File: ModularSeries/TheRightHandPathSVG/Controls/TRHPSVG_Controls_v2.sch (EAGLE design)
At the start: 56 parts, among them IC2 LM358

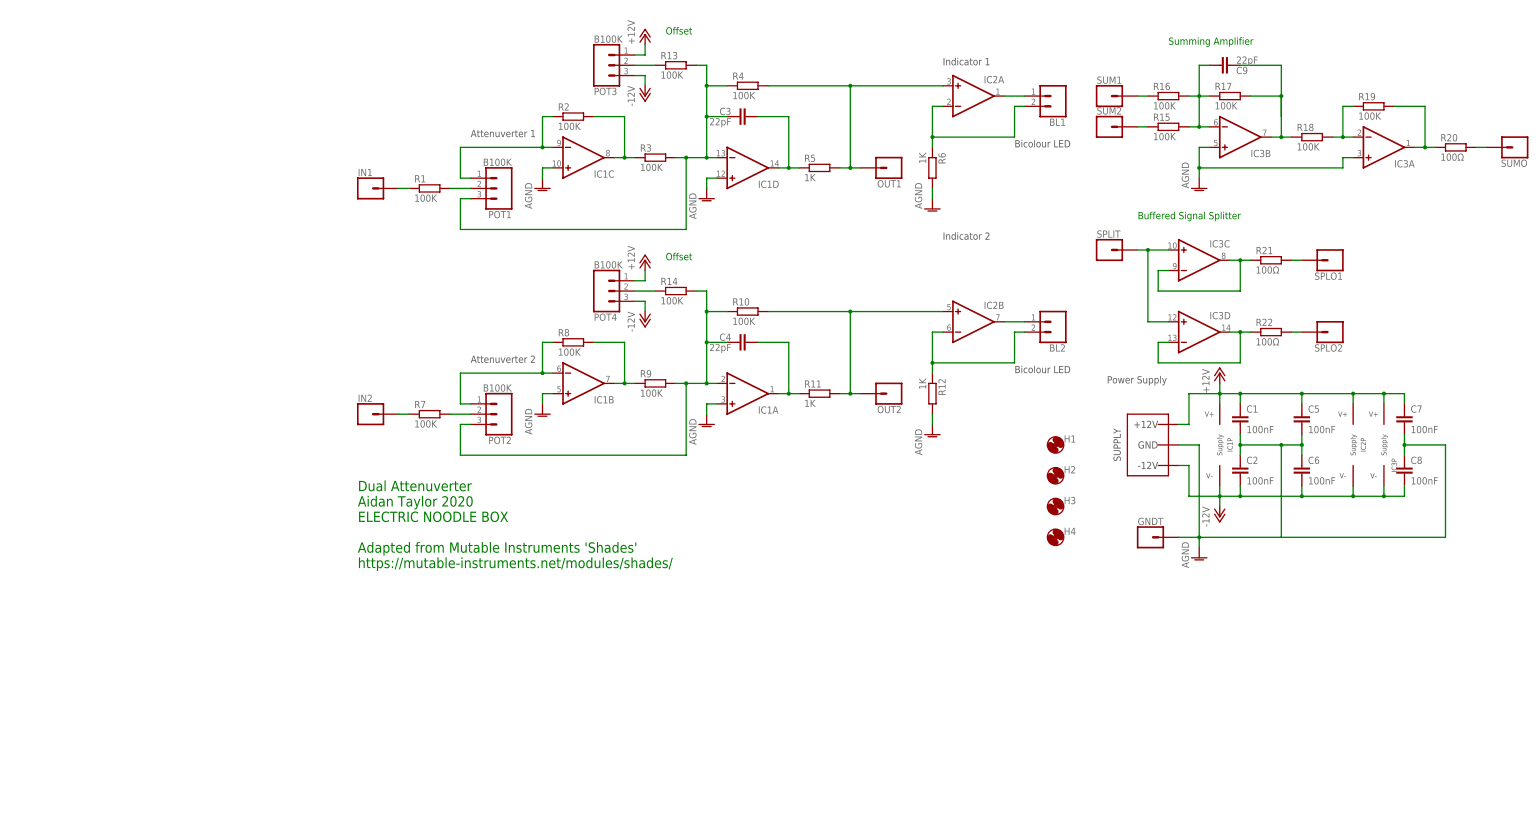
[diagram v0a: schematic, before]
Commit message: TRHP-SVG version 2, Endings added and Mirrors updated
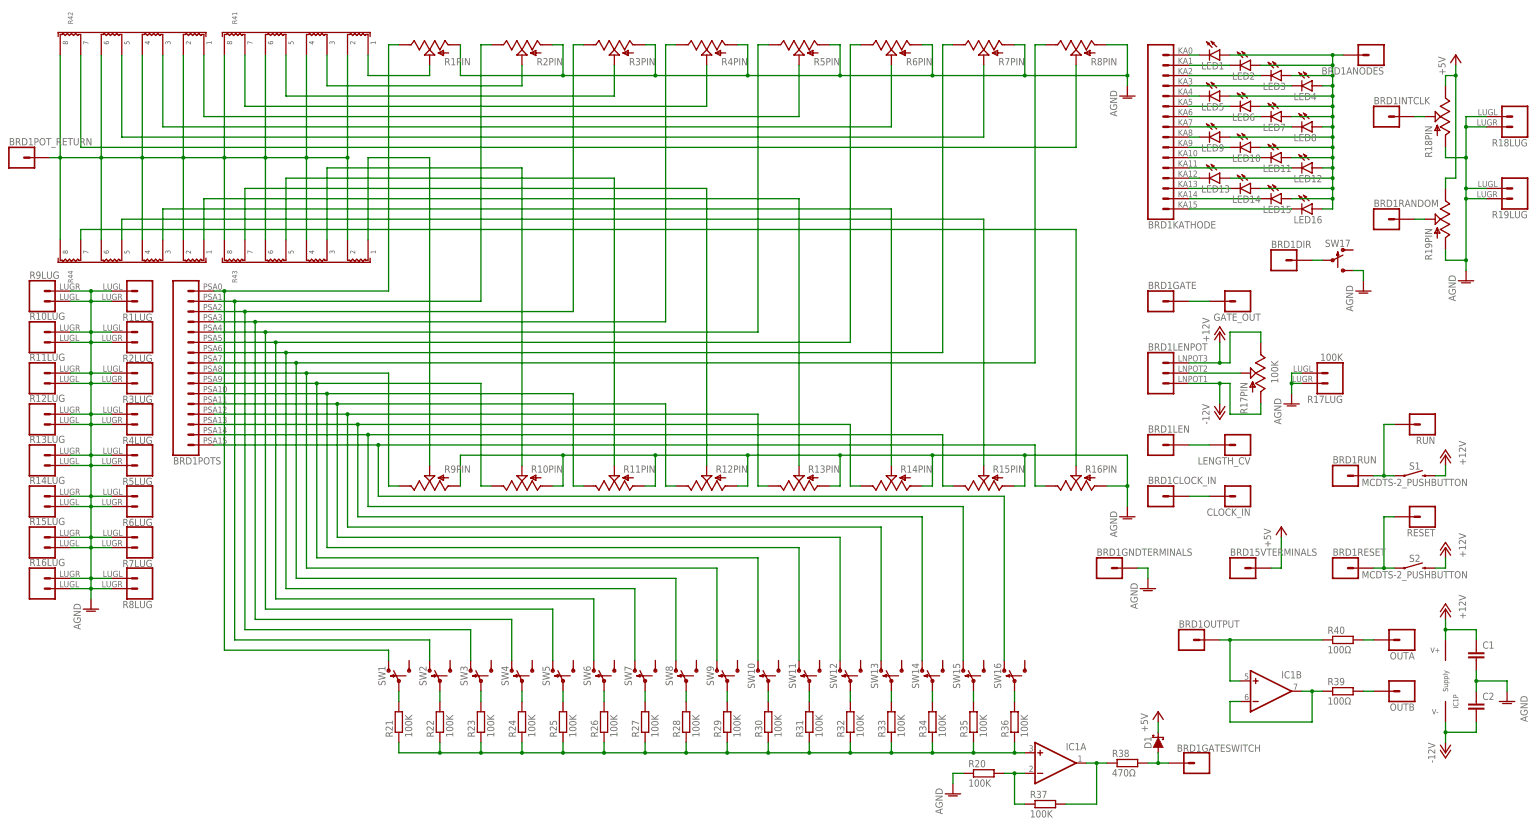
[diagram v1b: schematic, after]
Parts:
- removed BL1, BL2: 2XWIREPAD, ElectricNoodleBox:2XWIREPAD
- removed C3, C4, C9: 22pF, rcl:C-EU050-025X075
- removed C5, C6, C7, C8: 100nF, rcl:C-EU050-025X075
- removed GNDT, IN1, IN2, OUT1, OUT2, SPLIT, SPLO1, SPLO2, SUM1, SUM2, SUMO: 1XWIREPAD, ElectricNoodleBox:1XWIREPAD
- removed H1, H2, H3, H4: MOUNT-HOLE3.2, holes:MOUNT-HOLE3.2
- removed IC2: LM358, ElectricNoodleBox:LM358
- removed IC3: (no value), ElectricNoodleBox:TL0X4DIL
- removed POT1, POT2, POT3, POT4: B100K, ElectricNoodleBox:3XWIREPAD
- removed WP1: COMBO_SUPPLY_HEADER, ElectricNoodleBox:COMBO_SUPPLY_HEADER
- added BRD1: TRHPSVG_LINK, ElectricNoodleBox:TRHPSVG_LINK
- added CLOCK_IN, GATE_OUT, LENGTH_CV, OUTA, OUTB, RESET, RUN: BANANA_PANEL, ElectricNoodleBox:BANANA_PANEL
- added D1: (no value), ElectricNoodleBox:SCHOTTKY_DO35
- added LED1, LED10, LED11, LED12, LED13, LED14, LED15, LED16, LED2, LED3, LED4, LED5, LED6, LED7, LED8, LED9: (no value), led:LED3MM
- added R23, R24, R25, R26, R27, R28, R29, R30, R31, R32, R33, R34, R35, R36, R37: 100K, rcl:R-EU_0207/10
- added R38: 470Ω, rcl:R-EU_0207/10
- added R39, R40: 100Ω, rcl:R-EU_0207/10
- added R41, R42, R43, R44: (no value), ElectricNoodleBox:4XISO_RESISTOR_NETWORK_2.54
- added S1, S2: MCDTS-2_PUSHBUTTON, ElectricNoodleBox:MCDTS-2_PUSHBUTTON
- added SW1, SW10, SW11, SW12, SW13, SW14, SW15, SW16, SW17, SW2, SW3, SW4, SW5, SW6, SW7, SW8, SW9: SPDT_SWITCHDW1, ElectricNoodleBox:SPDT_SWITCHDW1
- C1, C2: value 100nF -> (none)
- IC1: device ElectricNoodleBox:TL0X4DIL -> ElectricNoodleBox:TL0X2DIL
- R1, R10, R13, R14, R15, R16, R18, R19, R2, R3, R4, R7, R8, R9: value 100K -> (none); device rcl:R-EU_0207/10 -> ElectricNoodleBox:POTENTIOMETER
- R11, R12, R5, R6: value 1K -> (none); device rcl:R-EU_0207/10 -> ElectricNoodleBox:POTENTIOMETER
- R17: device rcl:R-EU_0207/10 -> ElectricNoodleBox:POTENTIOMETER
- R20, R21, R22: value 100Ω -> 100K
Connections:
- new net +5V: BRD15VTERMINALS.1, D1.C, R18PIN.B, R19PIN.B
- new net N$33: BRD1KATHODE.1, LED1.C
- new net N$34: BRD1ANODES.1, LED1.A, LED10.A, LED11.A, LED12.A, LED13.A, LED14.A, LED15.A, LED16.A, LED2.A, LED3.A, LED4.A, LED5.A, LED6.A, LED7.A, LED8.A, LED9.A
- new net N$35: BRD1KATHODE.2, LED2.C
- new net N$36: BRD1KATHODE.3, LED3.C
- new net N$37: BRD1KATHODE.4, LED4.C
- new net N$38: BRD1KATHODE.5, LED5.C
- new net N$39: BRD1KATHODE.6, LED6.C
- new net N$40: BRD1KATHODE.7, LED7.C
- new net N$41: BRD1KATHODE.8, LED8.C
- new net N$42: BRD1KATHODE.9, LED9.C
- new net N$43: BRD1KATHODE.10, LED10.C
- new net N$44: BRD1KATHODE.11, LED11.C
- new net N$45: BRD1KATHODE.12, LED12.C
- new net N$46: BRD1KATHODE.13, LED13.C
- new net N$47: BRD1KATHODE.14, LED14.C
- new net N$48: BRD1KATHODE.15, LED15.C
- new net N$49: BRD1KATHODE.16, LED16.C
- new net N$50: BRD1LEN.1, LENGTH_CV.1
- new net N$51: BRD1CLOCK_IN.1, CLOCK_IN.1
- new net N$52: BRD1OUTPUT.1, IC1B.+IN, R40.1
- new net N$53: BRD1GATE.1, GATE_OUT.1
- new net N$54: BRD1DIR.1, SW17.P
- new net N$55: BRD1LENPOT.2, R17PIN.W
- new net N$56: BRD1POTS.6, R6PIN.B, SW6.O
- new net N$57: BRD1INTCLK.1, R18PIN.W
- new net N$58: BRD1RANDOM.1, R19PIN.W
- new net N$59: BRD1RUN.1, RUN.1, S1.1
- new net N$60: BRD1RESET.1, RESET.1, S2.1
- new net N$61: R26.2, SW6.P
- new net N$62: R27.2, SW7.P
- new net N$63: R28.2, SW8.P
- new net N$64: R29.2, SW9.P
- new net N$65: R30.2, SW10.P
- new net N$66: R31.2, SW11.P
- new net N$67: R32.2, SW12.P
- new net N$68: R33.2, SW13.P
- new net N$69: BRD1POTS.9, R9PIN.B, SW9.O
- new net N$70: BRD1POTS.11, R11PIN.B, SW11.O
- new net N$71: BRD1POTS.10, R10PIN.B, SW10.O
- new net N$72: BRD1POTS.13, R13PIN.B, SW13.O
- new net N$73: BRD1POTS.12, R12PIN.B, SW12.O
- new net N$74: R34.2, SW14.P
- new net N$75: R35.2, SW15.P
- new net N$76: IC1A.+IN, R21.1, R22.1, R23.1, R24.1, R25.1, R26.1, R27.1, R28.1, R29.1, R30.1, R31.1, R32.1, R33.1, R34.1, R35.1, R36.1
- new net N$77: IC1A.-IN, R20.2, R37.1
- new net N$78: IC1A.OUT, R37.2, R38.1
- new net N$79: BRD1GATESWITCH.1, D1.A, R38.2
- new net N$80: IC1B.-IN, IC1B.OUT, R39.1
- new net N$81: OUTB.1, R39.2
- new net N$82: OUTA.1, R40.2
- new net N$83: BRD1POT_RETURN.1, R41.P$2, R41.P$4, R41.P$6, R41.P$8, R42.P$2, R42.P$4, R42.P$6, R42.P$8, R43.P$2, R43.P$4, R43.P$6, R43.P$8, R44.P$2, R44.P$4, R44.P$6, R44.P$8
- net +12V: now also BRD1LENPOT.3, R17PIN.B, S1.2, S2.2; no longer C5.1, C7.1, IC2P.V+, IC3P.V+, POT3.1, POT4.1, WP1.V++
- net -12V: now also BRD1LENPOT.1, R17PIN.A; no longer C6.2, C8.2, IC2P.V-, IC3P.V-, POT3.3, POT4.3, WP1.V--
- net AGND: now also BRD1GNDTERMINALS.1, R10LUG.1, R10LUG.2, R10PIN.A, R11LUG.1, R11LUG.2, R11PIN.A, R12LUG.1, R12LUG.2, R12PIN.A, R13LUG.1, R13LUG.2, R13PIN.A, R14LUG.1, R14LUG.2, R14PIN.A, R15LUG.1, R15LUG.2, R15PIN.A, R16LUG.1, R16LUG.2, R16PIN.A, R17LUG.1, R17LUG.2, R18LUG.1, R18LUG.2, R18PIN.A, R19LUG.1, R19LUG.2, R19PIN.A, R1LUG.1, R1LUG.2, R1PIN.A, R20.1, R2LUG.1, R2LUG.2, R2PIN.A, R3LUG.1, R3LUG.2, R3PIN.A, R4LUG.1, R4LUG.2, R4PIN.A, R5LUG.1, R5LUG.2, R5PIN.A, R6LUG.1, R6LUG.2, R6PIN.A, R7LUG.1, R7LUG.2, R7PIN.A, R8LUG.1, R8LUG.2, R8PIN.A, R9LUG.1, R9LUG.2, R9PIN.A, SW17.S; no longer C5.2, C6.1, C7.2, C8.1, GNDT.1, IC1A.+IN, IC1B.+IN, IC1C.+IN, IC1D.+IN, IC3A.+IN, IC3B.+IN, R12.2, R6.2, WP1.AGND
- net N$1: now also R1PIN.W, R41.P$1; no longer POT1.2, R1.2
- net N$10: now also R42.P$7, R8PIN.W; no longer IC3A.-IN, R18.2, R19.1
- net N$11: now also BRD1POTS.3, R3PIN.B, SW3.O; no longer IC1B.-IN, POT2.1, R8.1
- net N$12: now also BRD1POTS.4, R4PIN.B, SW4.O; no longer IC1B.OUT, R8.2, R9.1
- net N$13: now also BRD1POTS.5, R5PIN.B, SW5.O; no longer C4.1, IC1A.-IN, POT2.3, R10.1, R14.2, R9.2
- net N$14: now also R36.2, SW16.P; no longer IC2B.+IN, OUT2.1, R10.2, R11.2
- net N$15: now also BRD1POTS.7, R7PIN.B, SW7.O; no longer C4.2, IC1A.OUT, R11.1
- net N$16: now also BRD1POTS.8, R8PIN.B, SW8.O; no longer IN2.1, R7.1
- net N$17: now also R43.P$1, R9PIN.W; no longer BL2.1, IC2B.OUT
- net N$18: now also R21.2, SW1.P; no longer BL2.2, IC2B.-IN, R12.1
- net N$19: now also R22.2, SW2.P; no longer BL1.2, IC2A.-IN, R6.1
- net N$2: now also R41.P$7, R4PIN.W; no longer IC1C.-IN, POT1.1, R2.1
- net N$20: now also R10PIN.W, R43.P$3; no longer POT3.2, R13.1
- net N$21: now also R23.2, SW3.P; no longer C9.2, IC3B.-IN, R15.2, R16.2, R17.1
- net N$22: now also R11PIN.W, R43.P$5; no longer POT4.2, R14.1
- net N$23: now also R12PIN.W, R43.P$7; no longer C9.1, IC3B.OUT, R17.2, R18.1
- net N$24: now also R24.2, SW4.P; no longer IC3A.OUT, R19.2, R20.1
- net N$25: now also R25.2, SW5.P; no longer R20.2, SUMO.1
- net N$26: now also R13PIN.W, R44.P$1; no longer R16.1, SUM1.1
- net N$27: now also R14PIN.W, R44.P$3; no longer R15.1, SUM2.1
- net N$28: now also BRD1POTS.14, R14PIN.B, SW14.O; no longer IC3C.-IN, IC3C.OUT, R21.1
- net N$29: now also BRD1POTS.15, R15PIN.B, SW15.O; no longer IC3D.-IN, IC3D.OUT, R22.1
- net N$3: now also R2PIN.W, R41.P$3; no longer POT2.2, R7.2
- net N$30: now also BRD1POTS.16, R16PIN.B, SW16.O; no longer IC3C.+IN, IC3D.+IN, SPLIT.1
- net N$31: now also R15PIN.W, R44.P$5; no longer R21.2, SPLO1.1
- net N$32: now also R16PIN.W, R44.P$7; no longer R22.2, SPLO2.1
- net N$4: now also BRD1POTS.1, R1PIN.B, SW1.O; no longer IC1C.OUT, R2.2, R3.1
- net N$5: now also BRD1POTS.2, R2PIN.B, SW2.O; no longer C3.1, IC1D.-IN, POT1.3, R13.2, R3.2, R4.1
- net N$6: now also R3PIN.W, R41.P$5; no longer IC2A.+IN, OUT1.1, R4.2, R5.2
- net N$7: now also R42.P$1, R5PIN.W; no longer C3.2, IC1D.OUT, R5.1
- net N$8: now also R42.P$3, R6PIN.W; no longer BL1.1, IC2A.OUT
- net N$9: now also R42.P$5, R7PIN.W; no longer IN1.1, R1.1
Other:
- note removed: "Attenuverter 1"
- note removed: "Attenuverter 2"
- note removed: "Bicolour LED"
- note removed: "Buffered Signal Splitter"
- note removed: "Dual Attenuverter Aidan Taylor 2020 ELECTRIC NOODLE BOX Adapted from Mutable Instruments 'Shades' https://mutable-instruments.net/modules/shades/"
- note removed: "Indicator 1"
- note removed: "Indicator 2"
- note removed: "Offset"
- note removed: "Power Supply"
- note removed: "Summing Amplifier"
- moved on the sheet: C1, C2, IC1A, IC1B, IC1P, R20, R21, R22

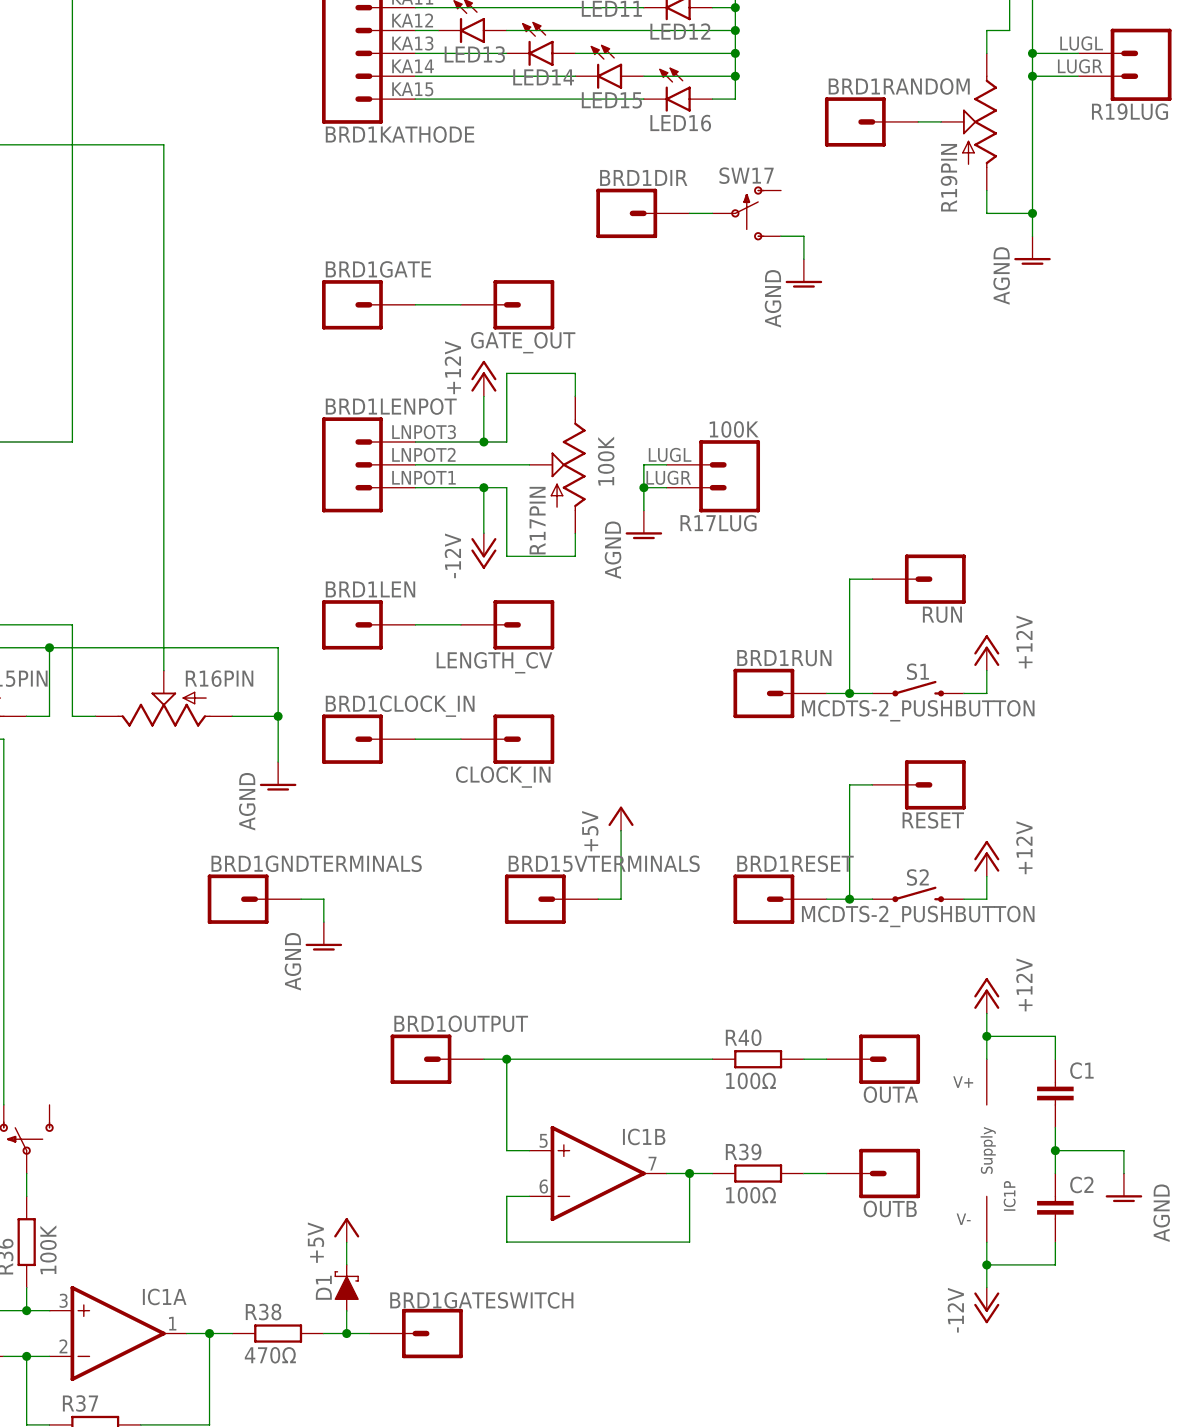
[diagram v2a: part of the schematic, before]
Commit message: Updates to Mirrors, Endings and TRHP SVG
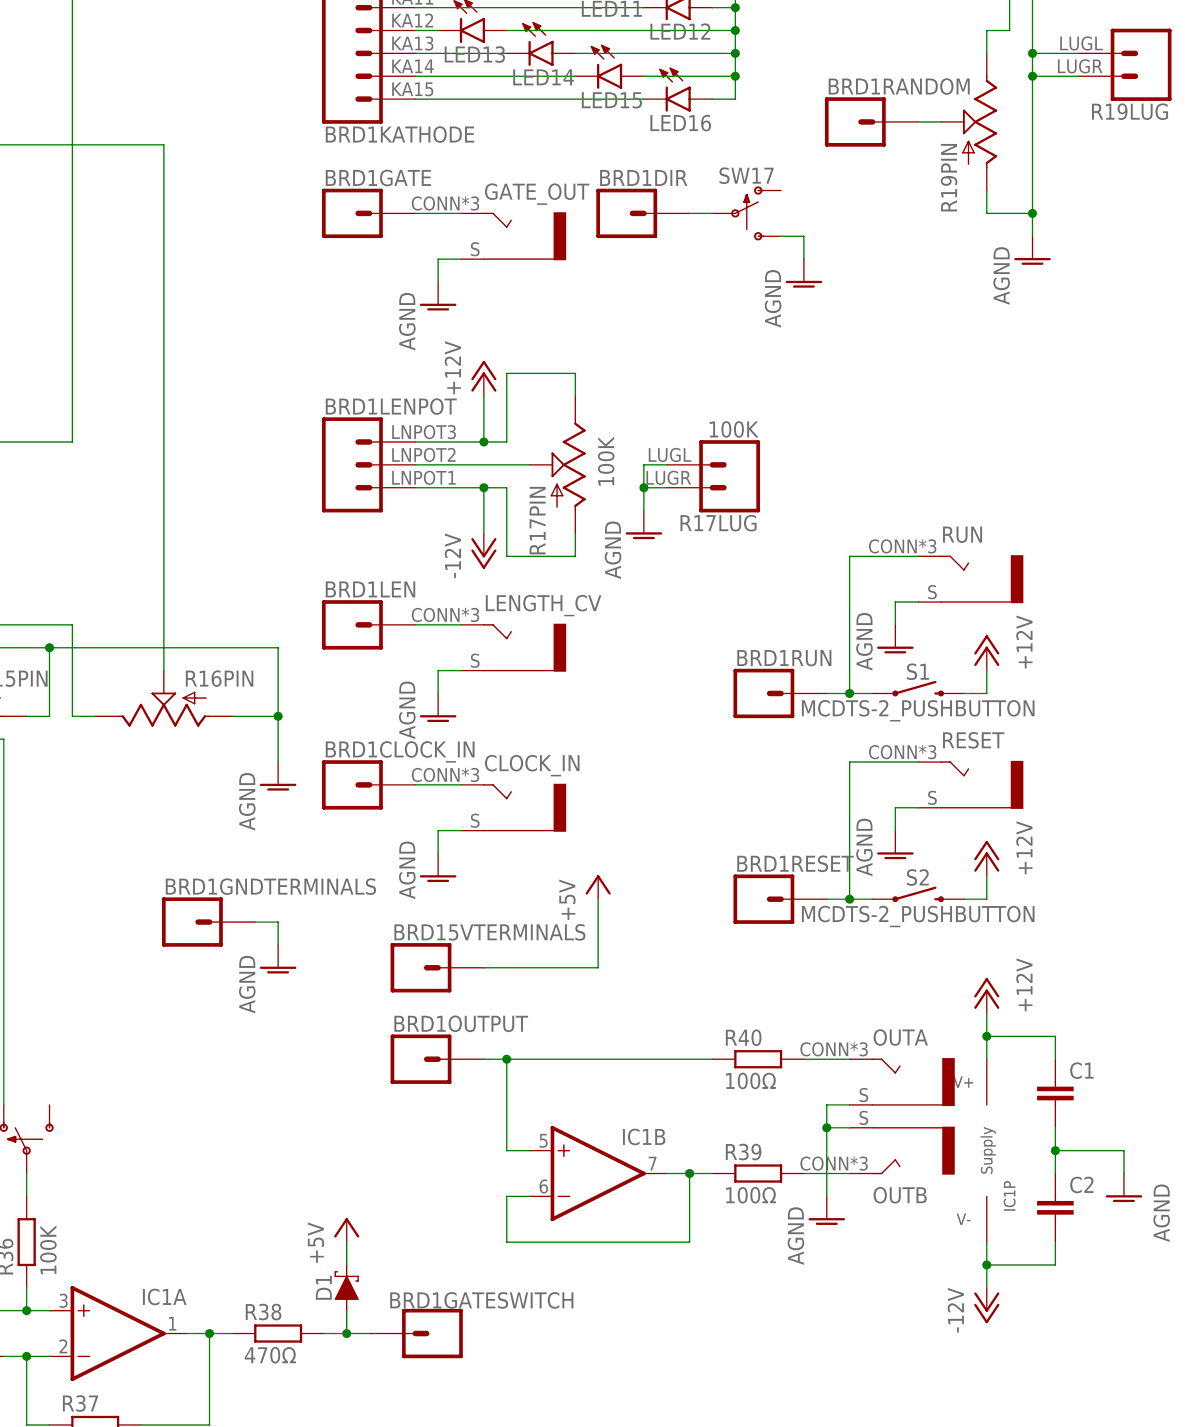
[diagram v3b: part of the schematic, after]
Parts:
- CLOCK_IN, GATE_OUT, LENGTH_CV, OUTA, OUTB, RESET, RUN: value BANANA_PANEL -> COMBI-JACK; device ElectricNoodleBox:BANANA_PANEL -> ElectricNoodleBox:COMBI-JACK
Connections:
- net AGND: now also CLOCK_IN.S, GATE_OUT.S, LENGTH_CV.S, OUTA.S, OUTB.S, RESET.S, RUN.S
- net N$50: now also LENGTH_CV.T; no longer LENGTH_CV.1
- net N$51: now also CLOCK_IN.T; no longer CLOCK_IN.1
- net N$53: now also GATE_OUT.T; no longer GATE_OUT.1
- net N$59: now also RUN.T; no longer RUN.1
- net N$60: now also RESET.T; no longer RESET.1
- net N$81: now also OUTB.T; no longer OUTB.1
- net N$82: now also OUTA.T; no longer OUTA.1
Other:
- moved on the sheet: BRD15VTERMINALS, BRD1CLOCK_IN, BRD1GATE, BRD1GNDTERMINALS
